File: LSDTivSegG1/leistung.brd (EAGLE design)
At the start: 160 x 100 mm, 80 parts, among them IC1 LM 2576 T5,0, IC2 IR2184D, IC3 IR2184D, IC4 4081N, IC5 4069N, IC6 LM 2576 T15, IC7 IR2184D, IC8 IR2184D, IC9 TINY13-20PU, X1 057-010-1, X2 MKDSN1,5/2-5,08

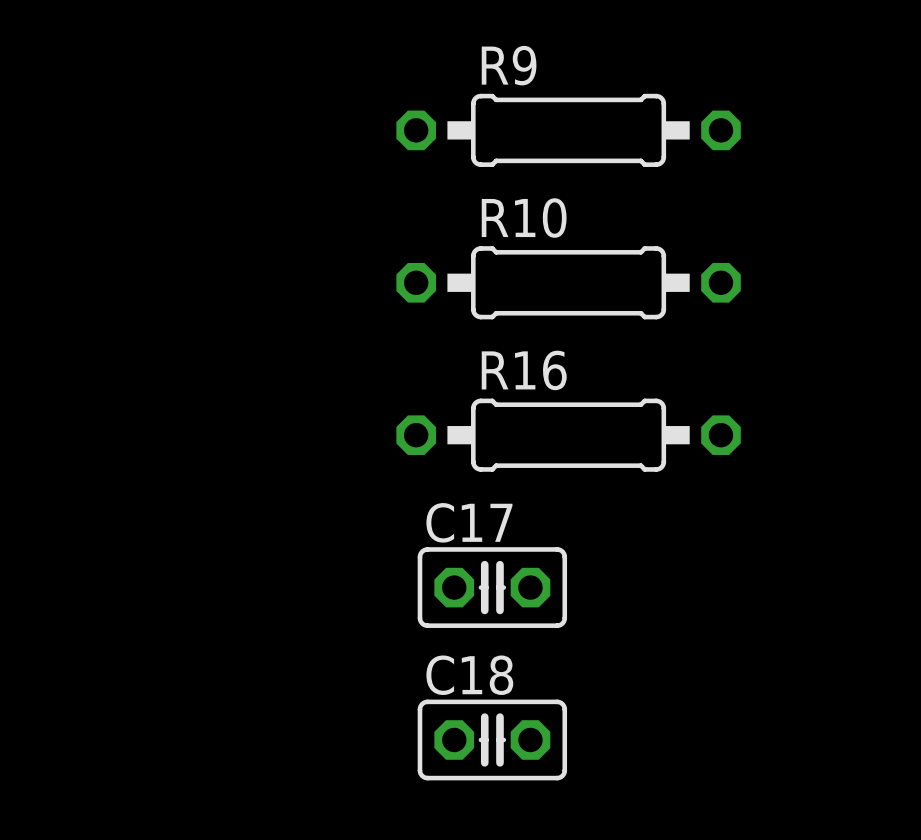
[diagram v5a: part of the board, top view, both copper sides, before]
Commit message: replaced resistor with potentiometer in voltage devider for battery monitoring
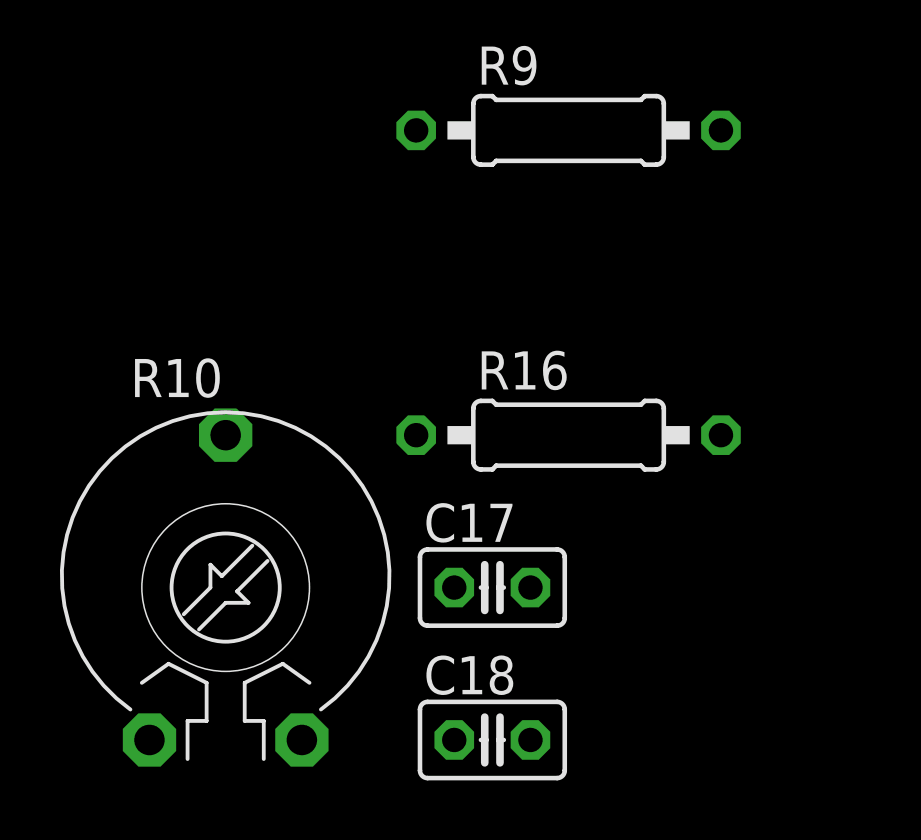
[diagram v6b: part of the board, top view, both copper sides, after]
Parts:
- R10: value 16k -> (none); device rcl:0207/10 -> rcl:PT-10
- moved R10 15.3 mm to (-55.9, -458.5)
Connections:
- net ADC: now also R10.3; no longer R10.2
- net GND: now also R10.2; no longer R10.1
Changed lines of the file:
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@@
 <element name="C16" library="rcl" package="C025-025X050" value="100n" x="-40.64" y="-435.61"/>
 <element name="R16" library="rcl" package="0207/10" value="82k" x="-44.45" y="-453.39"/>
-<element name="R10" library="rcl" package="0207/10" value="16k" x="-44.45" y="-448.31"/>
 <element name="C17" library="rcl" library_urn="urn:adsk.eagle:library:334" package="C025-025X050" package3d_urn="urn:adsk.eagle:package:23629/2" value="100nF" x="-46.99" y="-458.47">
 <attribute name="SPICEPREFIX" value="C" x="-46.99" y="-458.47" size="1.778" layer="27" display="off"/>
@@
 <element name="C18" library="rcl" library_urn="urn:adsk.eagle:library:334" package="C025-025X050" package3d_urn="urn:adsk.eagle:package:23629/2" value="100nF" x="-46.99" y="-463.55">
 <attribute name="SPICEPREFIX" value="C" x="-46.99" y="-463.55" size="1.778" layer="27" display="off"/>
+</element>
+<element name="R10" library="rcl" library_urn="urn:adsk.eagle:library:334" package="PT-10" package3d_urn="urn:adsk.eagle:package:23786/1" value="" x="-55.88" y="-458.47">
+<attribute name="SPICEMODEL" value="POT" x="-55.88" y="-458.47" size="1.778" layer="27" display="off"/>
+<attribute name="SPICEPREFIX" value="X" x="-55.88" y="-458.47" size="1.778" layer="27" display="off"/>
 </element>
 </elements>
@@
 <contactref element="C10" pad="1"/>
 <contactref element="C16" pad="2"/>
-<contactref element="R10" pad="1"/>
 <contactref element="U$1" pad="4A"/>
 <contactref element="U$1" pad="4B"/>
@@
 <contactref element="C18" pad="2"/>
 <contactref element="C17" pad="2"/>
+<contactref element="R10" pad="2"/>
 <wire x1="-45.72" y1="-463.55" x2="-45.72" y2="-458.47" width="0" layer="19" extent="1-1"/>
-<wire x1="-49.53" y1="-448.31" x2="-45.72" y2="-458.47" width="0" layer="19" extent="1-1"/>
-<wire x1="-48.26" y1="-435.61" x2="-49.53" y2="-448.31" width="0" layer="19" extent="1-1"/>
+<wire x1="-53.34" y1="-463.55" x2="-45.72" y2="-463.55" width="0" layer="19" extent="1-1"/>
+<wire x1="-48.26" y1="-435.61" x2="-45.72" y2="-458.47" width="0" layer="19" extent="1-1"/>
 <wire x1="-39.37" y1="-435.61" x2="-48.26" y2="-435.61" width="0" layer="19" extent="1-1"/>
 <wire x1="-38.1" y1="-430.53" x2="-39.37" y2="-435.61" width="0" layer="19" extent="1-1"/>
@@
 <contactref element="IC9" pad="3"/>
 <contactref element="R16" pad="1"/>
-<contactref element="R10" pad="2"/>
-<wire x1="-39.37" y1="-448.31" x2="-49.53" y2="-453.39" width="0" layer="19" extent="1-1"/>
-<wire x1="-40.64" y1="-430.53" x2="-39.37" y2="-448.31" width="0" layer="19" extent="1-1"/>
+<contactref element="R10" pad="3"/>
+<wire x1="-55.88" y1="-453.39" x2="-49.53" y2="-453.39" width="0" layer="19" extent="1-1"/>
+<wire x1="-40.64" y1="-430.53" x2="-49.53" y2="-453.39" width="0" layer="19" extent="1-1"/>
 </signal>
 </signals>

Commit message: Nachbesprechung Änderungen gemacht
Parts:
- added C19, C20: 4m7, rcl:E7,5-18
- added R11, R12, R13, R25: 470k, rcl:0207/7
- C1, C11: value 10u -> 4m7; device rcl:E2,5-5 -> rcl:E7,5-18
- D1, D13, D14, D2: value 1N4001 -> 1N4002
- D15, D16, D17, D18, D3, D4, D5, D6: value 18 -> ZD-5W_18V
- D7, D8: value 1N 5711 -> 1N5822
- Q1, Q10, Q11, Q12, Q2, Q3, Q4, Q9: value (none) -> IRFB3077
- R10: value (none) -> 20k
- moved C1 487.7 mm to (-52.1, -548.6)
- moved C11 183.9 mm to (-52.1, -510.5)
- moved IC8 1.27 mm to (-30.5, -295.9)
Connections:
- removed net BAT_PWM_IN: IC9.5
- removed net DIRL_IN_INV: IC5.2
- removed net DIRR_IN_INV: IC5.4
- removed net MOTOR_L_ACTIVE: IC2.2, IC3.2, IC4.3
- removed net MOTOR_R_ACTIVE: IC4.4, IC7.2, IC8.2
- removed net N$15: IC4.10
- removed net N$16: IC4.11
- removed net N$21: IC4.8
- removed net N$22: IC4.9
- removed net N$23: IC4.12
- removed net N$24: IC4.13
- removed net N$29: D16.C, Q10.G, R18.2, R23.1
- new net IN_L: IC2.1, IC4.4
- new net IN_L_INVD: IC3.1, IC4.11
- new net IN_R: IC4.3, IC7.1
- new net IN_R_INVD: IC4.10, IC8.1
- new net N$13: D16.C, Q10.G, R18.2, R23.2
- net BAT_+: now also C19.+, C20.+
- net BAT_PWM: now also IC9.5
- net DIRL: now also IC4.5, IC5.3; no longer IC2.1, IC5.1
- net DIRL_INV: now also IC4.12, IC5.4; no longer IC3.1
- net DIRR: now also IC4.1, IC5.1; no longer IC5.3, IC7.1
- net DIRR_INV: now also IC4.8, IC5.2; no longer IC8.1
- net ENABLE: now also IC2.2, IC3.2, IC7.2, IC8.2, R11.2, R12.2, R13.2, R25.2; no longer IC4.1, IC4.5
- net GND: now also C19.-, C20.-, D16.A, D17.A, D4.A, D5.A, R11.1, R12.1, R13.1, R22.1, R23.1, R25.1, R6.1, R7.1
- net MOTOR_L_+: no longer D4.A, R7.2
- net MOTOR_L_-: no longer D5.A, R6.2
- net MOTOR_PWM_L: now also IC4.13, IC4.6; no longer IC4.2
- net MOTOR_PWM_R: now also IC4.2, IC4.9; no longer IC4.6
- net MOTOR_R_+: no longer D16.A, R23.2
- net MOTOR_R_-: no longer D17.A, R22.2
- net N$32: now also R22.2; no longer R22.1
- net N$5: now also R7.2; no longer R7.1
- net N$8: now also R6.2; no longer R6.1

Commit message: eagle 7 export
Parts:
- added U$2: (no value), lsd2016:BOARD
- C6: device rcl:E2,5-4R -> rcl:E5-13
- moved C19 765.1 mm to (59.7, 189.2), turned to 270 degrees
- moved C20 718.9 mm to (175.3, 152.4)
- moved C11 711.0 mm to (73.7, 189.2), turned to 270 degrees
- moved R12 649.5 mm to (125.7, 134.6), turned to 180 degrees
- moved C1 641.0 mm to (44.5, 85.1), turned to 270 degrees
- moved R11 639.8 mm to (97.8, 137.2), turned to 180 degrees
- moved R25 564.4 mm to (71.1, 50.8), turned to 270 degrees
- moved R13 552.4 mm to (67.3, 44.5)
- moved C6 542.3 mm to (232.4, 94.0)
- moved C18 538.0 mm to (106.7, 52.1), turned to 90 degrees
- moved R19 529.4 mm to (137.2, 163.8)
- moved R18 523.6 mm to (104.1, 165.1), turned to 180 degrees
- moved R20 520.9 mm to (119.4, 163.8)
- moved C7 518.2 mm to (209.6, 85.1)
- moved D7 518.2 mm to (207.0, 90.2)
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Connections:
- removed net NC2: X1.10
- removed net VB: C12.+, C13.+, C2.+, C3.+, D1.C, D13.C, D14.C, D2.C, IC2.8, IC3.8, IC7.8, IC8.8
- new net VB1: C2.+, D1.C, IC2.8
- new net VB2: C3.+, D2.C, IC3.8
- new net VB3: C12.+, D13.C, IC7.8
- new net VB4: C13.+, D14.C, IC8.8
- net +24V: now also X1.10
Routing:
- net MOTOR_L_+: track 0.00 -> 28.0 mm
- net +15V: track 0.00 -> 23.2 mm
- net VB1: track 0.00 -> 15.5 mm
- net ENABLE: track 0.00 -> 9.42 mm
- net MOTOR_R_-: track 0.00 -> 7.62 mm
- net MOTOR_R_+: track 0.00 -> 7.62 mm
- net MOTOR_L_-: track 0.00 -> 7.62 mm
- net BAT_+: track 0.00 -> 7.62 mm
- net N$10: track 0.00 -> 7.40 mm
- net IN_L: track 0.00 -> 6.88 mm
- net N$5: track 0.00 -> 6.13 mm
- net N$6: track 0.00 -> 5.08 mm
- net GND: track 0.00 -> 2.54 mm
- net N$9: track 0.00 -> 2.54 mm
- added copper zone on layer 1, net BAT_+
- added copper zone on layer 16, net GND
